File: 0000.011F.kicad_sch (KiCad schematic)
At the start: 24 parts, among them J3 BH254, J5 BH254, U3 TL072

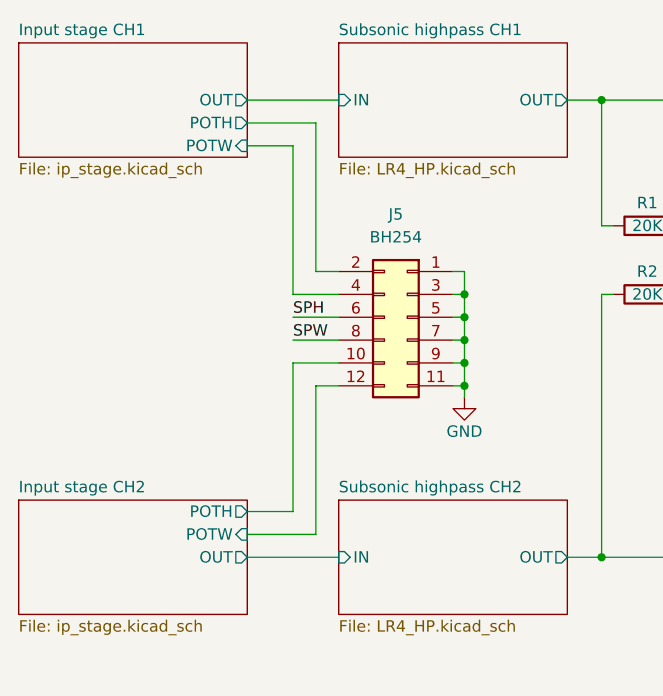
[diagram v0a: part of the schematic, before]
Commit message: Pot board made smaller using MicroMatch connectors. Snap-off holes tidied up, and gap increased to 2mm for compatibility with some PCB manufacturer's design rules.
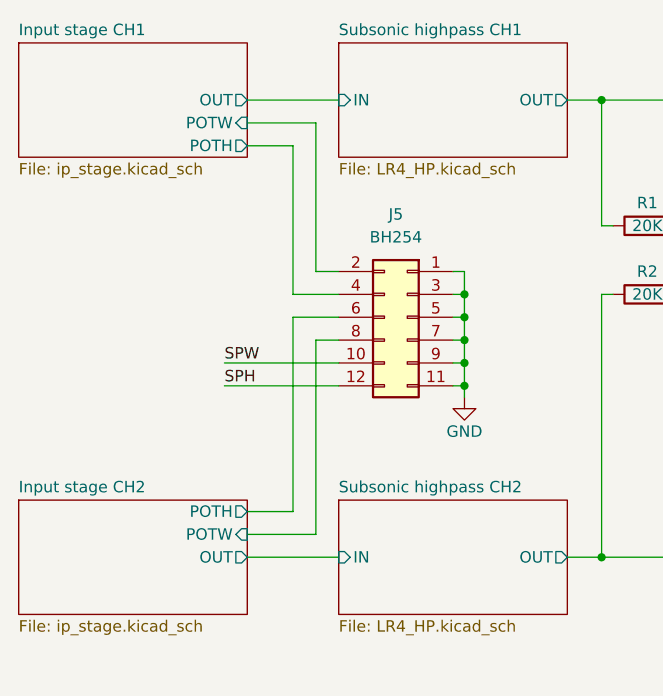
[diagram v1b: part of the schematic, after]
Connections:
- net Input stage CH1/POTH: now also J5.4 (Pin_4); no longer J5.2 (Pin_2)
- net Input stage CH1/POTW: now also J5.2 (Pin_2); no longer J5.4 (Pin_4)
- net Input stage CH2/POTH: now also J5.6 (Pin_6); no longer J5.10 (Pin_10)
- net Input stage CH2/POTW: now also J5.8 (Pin_8); no longer J5.12 (Pin_12)
- net SPH: now also J5.12 (Pin_12); no longer J5.6 (Pin_6)
- net SPW: now also J5.10 (Pin_10); no longer J5.8 (Pin_8)
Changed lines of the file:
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@@
 	(wire
 		(pts
-			(xy 71.12 102.87) (xy 71.12 86.36)
+			(xy 71.12 81.28) (xy 71.12 102.87)
 		)
 		(stroke
@@
 	(wire
 		(pts
-			(xy 71.12 81.28) (xy 76.2 81.28)
+			(xy 63.5 88.9) (xy 76.2 88.9)
 		)
 		(stroke
@@
 	(wire
 		(pts
-			(xy 71.12 83.82) (xy 76.2 83.82)
+			(xy 63.5 86.36) (xy 76.2 86.36)
 		)
 		(stroke
@@
 	(wire
 		(pts
-			(xy 73.66 88.9) (xy 76.2 88.9)
-		)
-		(stroke
-			(width 0)
-			(type default)
-		)
-	)
-	(wire
-		(pts
-			(xy 73.66 105.41) (xy 73.66 88.9)
-		)
-		(stroke
-			(width 0)
-			(type default)
-		)
-	)
-	(wire
-		(pts
 			(xy 147.32 81.28) (xy 154.94 81.28)
 		)
@@
 	(wire
 		(pts
+			(xy 76.2 81.28) (xy 71.12 81.28)
+		)
+		(stroke
+			(width 0)
+			(type default)
+		)
+	)
+	(wire
+		(pts
 			(xy 127 152.4) (xy 127 165.1)
 		)
@@
 	(wire
 		(pts
+			(xy 76.2 83.82) (xy 73.66 83.82)
+		)
+		(stroke
+			(width 0)
+			(type default)
+		)
+	)
+	(wire
+		(pts
 			(xy 111.76 152.4) (xy 119.38 152.4)
 		)
@@
 	(wire
 		(pts
-			(xy 71.12 86.36) (xy 76.2 86.36)
+			(xy 133.35 140.97) (xy 133.35 144.78)
 		)
 		(stroke
@@
 	(wire
 		(pts
-			(xy 133.35 140.97) (xy 133.35 144.78)
+			(xy 73.66 83.82) (xy 73.66 105.41)
 		)
 		(stroke
@@
 	)
 	(label "SPH"
-		(at 71.12 81.28 0)
+		(at 63.5 88.9 0)
 		(effects
 			(font
@@
 	)
 	(label "SPW"
-		(at 71.12 83.82 0)
+		(at 63.5 86.36 0)
 		(effects
 			(font
@@
 		)
 		(pin "POTH" output
-			(at 66.04 59.69 0)
+			(at 66.04 62.23 0)
 			(effects
 				(font
@@
 		)
 		(pin "POTW" input
-			(at 66.04 62.23 0)
+			(at 66.04 59.69 0)
 			(effects
 				(font
